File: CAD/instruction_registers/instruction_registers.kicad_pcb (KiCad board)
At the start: 2 copper layers, 100 x 60 mm, 63 parts, among them J1 Conn_01x32_Pin, J2 Conn_01x06_Pin, SW1 SW_Push, SW2 SW_Push, SW3 SW_SPDT, U1 74HC377, U2 74HC377, U3 74HC377, U4 74HC245, U5 74HC245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

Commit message: update KiCAD version 10.0
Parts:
- removed G***: LOGO, 8-bit_computer:qr-code-github

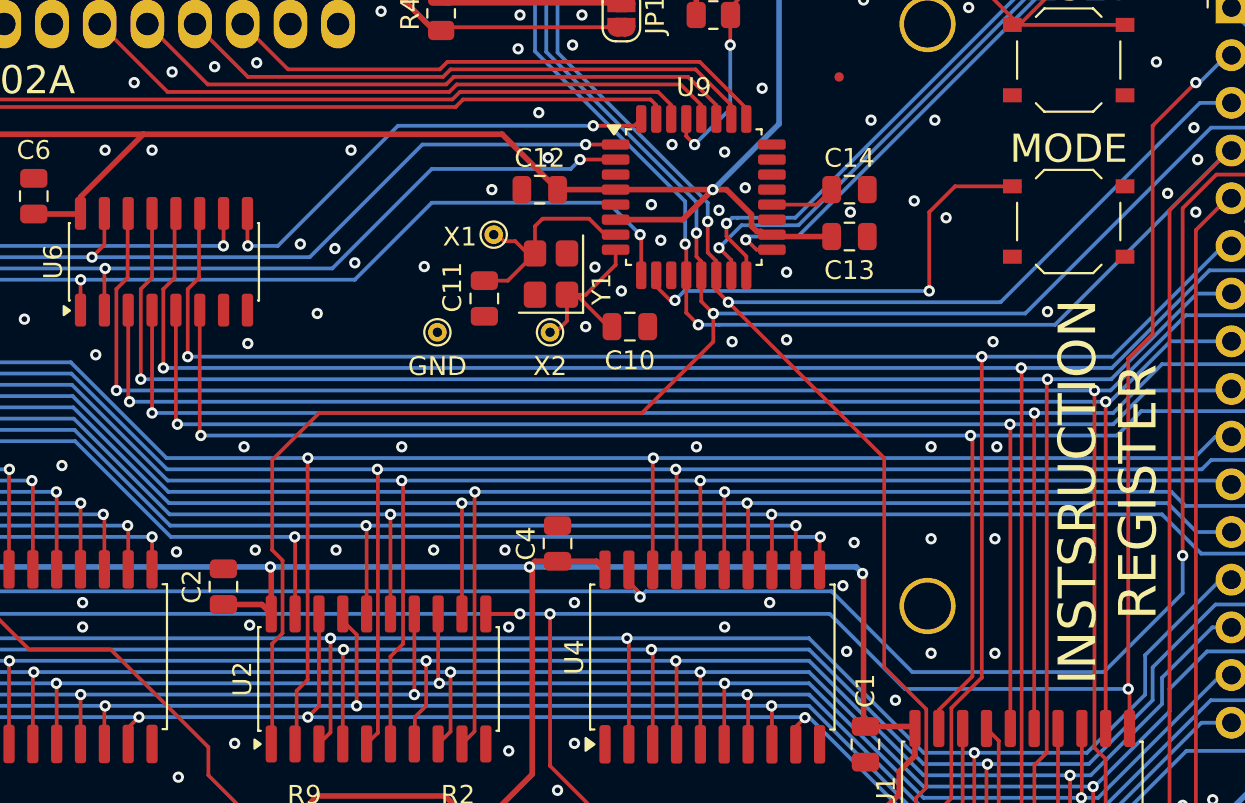
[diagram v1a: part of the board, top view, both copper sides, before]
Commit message: exclude known warnings in ERC and DRC
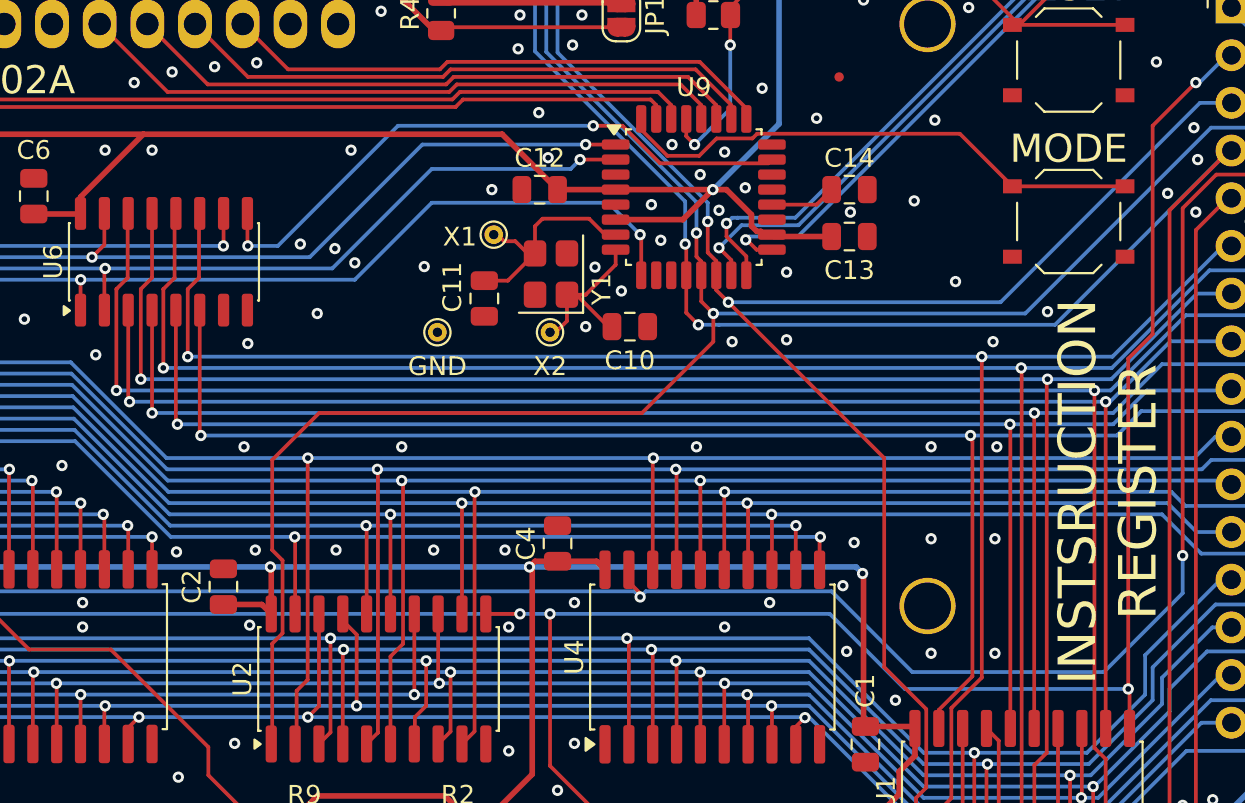
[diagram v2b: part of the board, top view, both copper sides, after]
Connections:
- U9 pad 10: ~{sw_mode} -> unconnected-(U9-PD6-Pad10)
- U9 pad 23: unconnected-(U9-PC0-Pad23) -> ser_in
- U9 pad 32: ser_in -> ~{sw_mode}
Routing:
- net ser_in: track 25.5 -> 33.2 mm
- net ~{sw_mode}: track 24.7 -> 28.0 mm, vias 2 -> 0
- net GND: vias 148 -> 149
